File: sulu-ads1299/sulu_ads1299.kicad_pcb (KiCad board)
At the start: 2 copper layers, 32.5 x 42.8 mm, 76 parts, among them J1 Conn_01x08, J11 through_hole, J16 through_hole, J17 through_hole, J2 Conn_01x02, J20 through_hole, J3 Conn_02x05_Odd_Even, J4 through_hole, J5 through_hole, J6 through_hole, J8 through_hole, SW1 SW_DIP_x02, U1 TPS62222DDCT, U2 TLV71311PDBV, U3 LM2775DSG, U4 ADS1299_TQFP-64, U5 scum3

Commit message: Final submitted layout, gerbers, drill files, bom, and cpl
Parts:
- L2: footprint Inductor_SMD:L_Wuerth_MAPI-2010 -> Inductor_SMD:L_1008_2520Metric
- SW1: footprint Button_Switch_SMD:SW_DIP_SPSTx02_Slide_6.7x6.64mm_W6.73mm_P2.54mm_LowProfile_JPin -> eec:CK_Components-TDA02H0SB1-MFG
- moved U2 0.77 mm to (89.3, 68.7)
- moved C9 0.77 mm to (86.6, 68.2)
- moved C10 0.57 mm to (92.2, 68.2)
- moved L2 0.33 mm to (93.0, 72.1)
- moved SW1 0.13 mm to (113.2, 88.9)
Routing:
- net +1.8V_REG: track 86.1 -> 84.5 mm
- net +EXT_BAT: track 79.4 -> 78.1 mm
- net /~{ADS_PWDN}: track 22.1 -> 21.6 mm

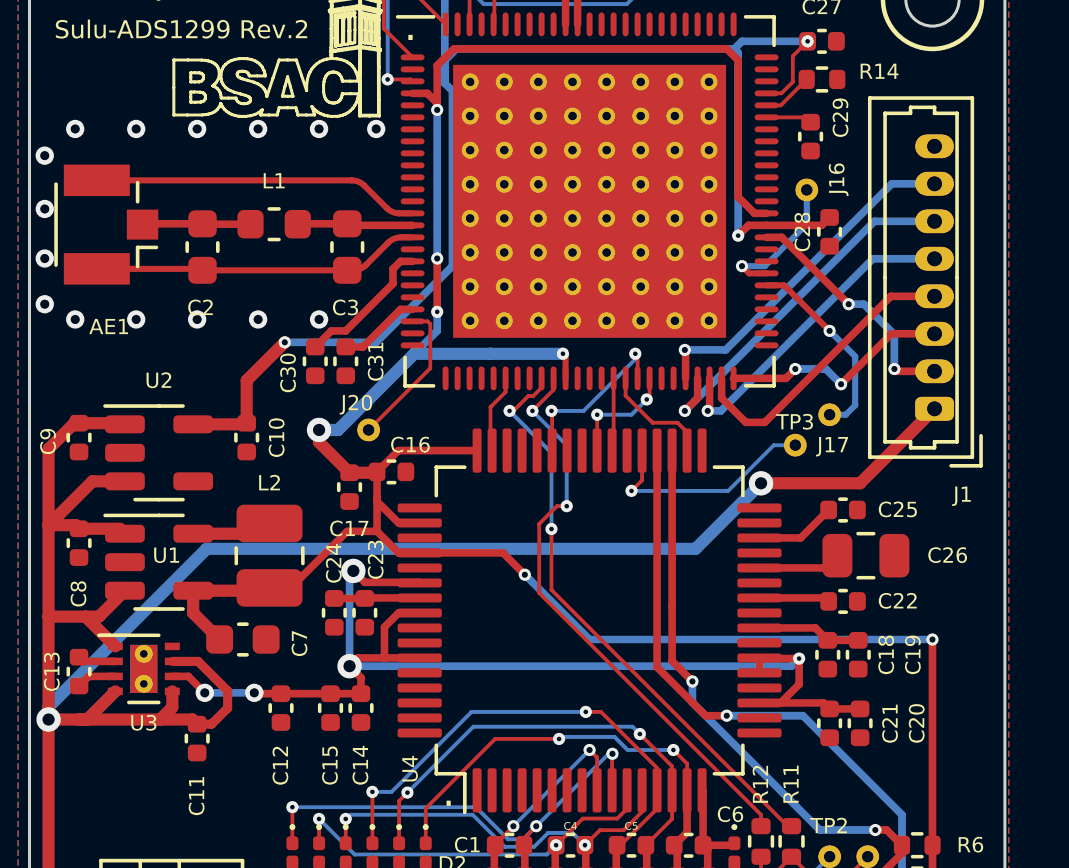
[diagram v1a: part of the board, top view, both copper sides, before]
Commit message: Sulu-ADS1299 Rev 3 improved routing surrounding QFN
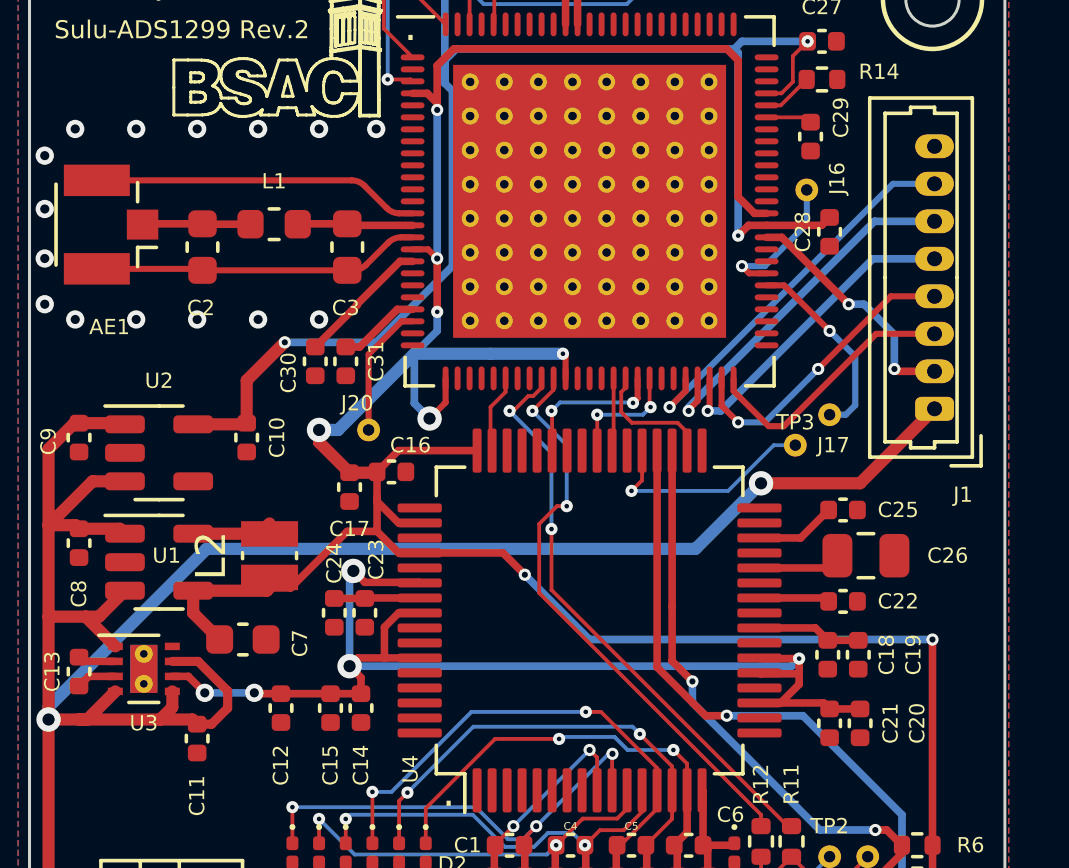
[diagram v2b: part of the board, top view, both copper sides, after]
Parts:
- L2: footprint Inductor_SMD:L_1008_2520Metric -> Inductor_SMD:L_Wuerth_MAPI-2010
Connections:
- U5 pad 17: unconnected-(U5-Pad17) -> +1.8V_REG
- U5 pad 26: unconnected-(U5-Pad26) -> +1.8V_REG
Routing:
- net +1.8V_REG: track 84.5 -> 89.3 mm, vias 7 -> 8
- net /RsTx: track 11.6 -> 13.1 mm
- net /3WB_DATA: track 7.73 -> 8.88 mm, vias 2 -> 0
- net +5V_REG: track 40.9 -> 41.7 mm
- net /SCUM_GPIO13: track 5.87 -> 5.05 mm
- net Net-(J20-Pad1): track 5.01 -> 4.44 mm
- net /SCUM_GPIO12: track 3.74 -> 4.27 mm
- net /3WB_ENB: track 9.83 -> 9.98 mm, vias 0 -> 2

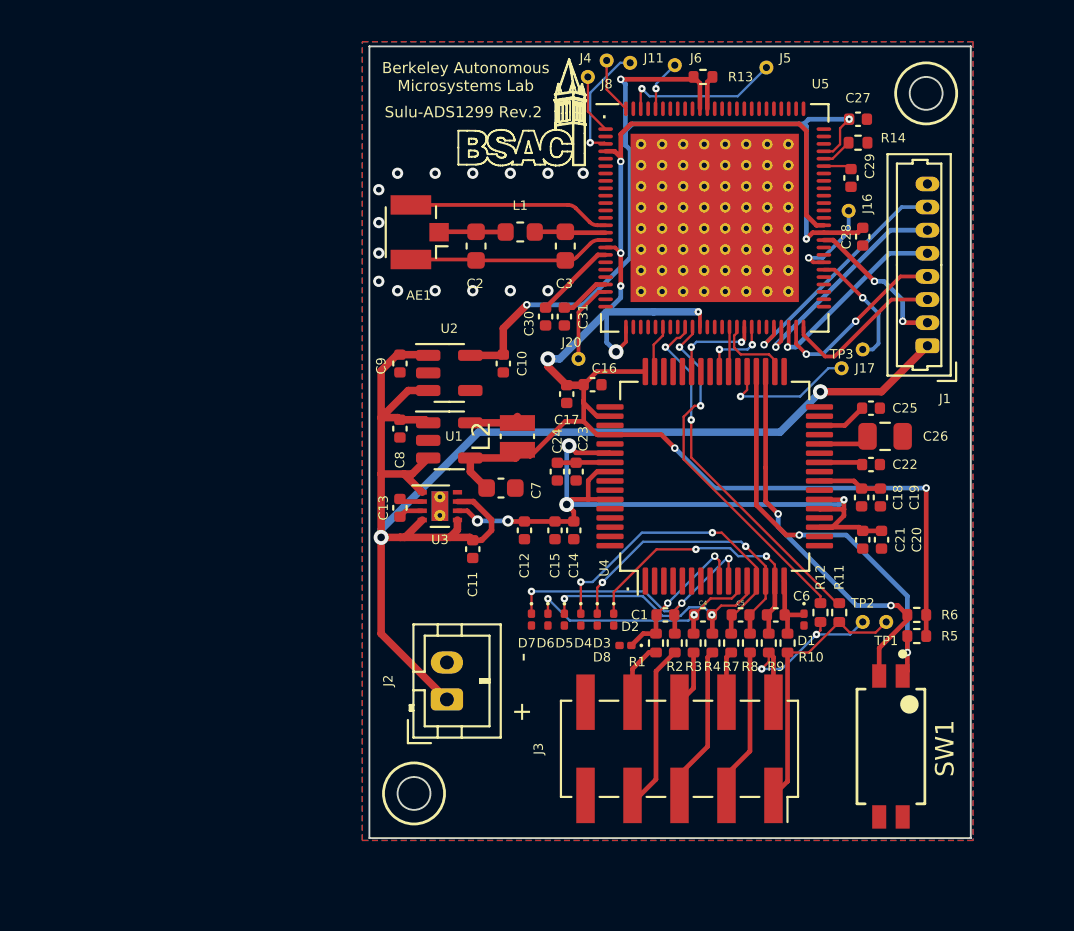
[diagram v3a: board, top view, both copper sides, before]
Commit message: Sulu-ADS1299 rev 3 fixed gpios, debug connector, two regulators
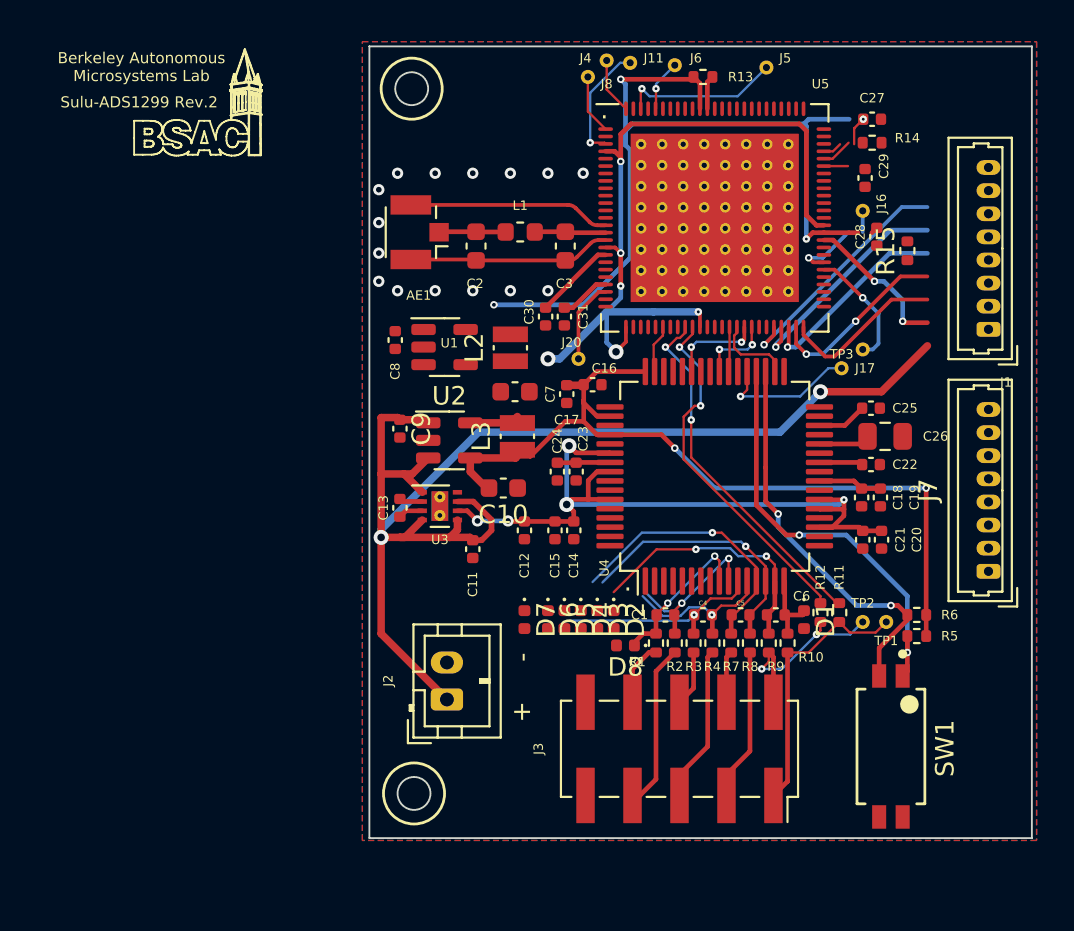
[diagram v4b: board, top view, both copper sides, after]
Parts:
- added J7: Conn_01x08, Molex Connectors:Molex_PicoBlade_53047-0810_1x08_P1.25mm_Vertical, F.Cu at (118.4, 79.4)
- added L3: 4.7 uH, Inductor_SMD:L_Wuerth_MAPI-2010, F.Cu at (93.0, 72.1)
- added R15: NP, Resistor_SMD:R_0402_1005Metric, F.Cu at (114.0, 62.1)
- C10: value 0.1 uF -> 22 uF; footprint Capacitor_SMD:C_0402_1005Metric -> Capacitor_SMD:C_0603_1608Metric
- C9: value 0.1 uF -> 4.7 uF
- D1, D2, D3, D4, D5, D6, D7, D8: footprint Diode_SMD:D_0201_0603Metric -> Diode_SMD:D_0402_1005Metric
- U2: value TLV71311PDBV -> TPS62222DDCT
- moved C10 6.73 mm to (92.2, 74.9), turned to 180 degrees
- moved C7 5.26 mm to (92.8, 69.7)
- moved U1 5.05 mm to (89.0, 67.3)
- moved L2 4.80 mm to (92.6, 67.3)
- moved C8 4.80 mm to (86.4, 66.9)
- moved U2 3.65 mm to (89.3, 72.4)
- moved C9 3.52 mm to (86.6, 71.7)
- moved J1 3.42 mm to (118.4, 66.4)
- moved C27 0.76 mm to (112.1, 55.0)
- moved C28 0.76 mm to (112.4, 61.3)
- moved C29 0.76 mm to (111.8, 58.2)
- moved J16 0.76 mm to (111.6, 59.9)
- moved R14 0.76 mm to (112.1, 56.3)
- moved D7 0.38 mm to (93.3, 82.0)
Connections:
- C10 pad 1: +1.1V_REG -> GND
- C10 pad 2: GND -> /+1.8V_ADS
- C16 pad 1: +1.8V_REG -> /+1.8V_ADS
- C17 pad 1: +1.8V_REG -> /+1.8V_ADS
- C27 pad 1: +1.1V_REG -> /SCuM-3C/+1.1V_REG
- C28 pad 1: +1.1V_REG -> /SCuM-3C/+1.1V_REG
- C7 pad 2: +1.8V_REG -> /+1.8V_SCUM
- L2 pad 1: +1.8V_REG -> /+1.8V_SCUM
- R11 pad 1: /SCUM_GPIO6 -> /SCUM_GPIO9
- R12 pad 1: /SCUM_GPIO7 -> /SCUM_GPIO10
- R13 pad 1: +1.1V_REG -> Net-(R13-Pad1)
- R5 pad 1: +1.8V_REG -> /+1.8V_SCUM
- R5 pad 2: /~{ADS_RESET} -> /SCUM_GPIO5
- R6 pad 1: +1.8V_REG -> /+1.8V_SCUM
- SW1 pad 1: /~{ADS_RESET} -> /SCUM_GPIO5
- U1 pad 4: +1.8V_REG -> /+1.8V_SCUM
- U2 pad 4: unconnected-(U2-Pad4) -> /+1.8V_ADS
- U2 pad 5: +1.1V_REG -> Net-(L3-Pad2)
- U4 pad 34: /SCUM_GPIO12 -> /SCUM_GPIO7
- U4 pad 36: /~{ADS_RESET} -> /SCUM_GPIO5
- U4 pad 39: /SCUM_GPIO11 -> /SCUM_GPIO4
- U4 pad 48: +1.8V_REG -> /+1.8V_ADS
- U4 pad 50: +1.8V_REG -> /+1.8V_ADS
- U4 pad 52: +1.8V_REG -> /+1.8V_ADS
- U5 pad 17: +1.8V_REG -> /+1.8V_SCUM
- U5 pad 26: +1.8V_REG -> /+1.8V_SCUM
- U5 pad 36: +1.8V_REG -> /+1.8V_SCUM
- U5 pad 4: +1.8V_REG -> /+1.8V_SCUM
- U5 pad 59: unconnected-(U5-Pad59) -> /+1.8V_SCUM
- U5 pad 61: +1.1V_REG -> /SCuM-3C/+1.1V_REG
- U5 pad 62: +1.8V_REG -> /+1.8V_SCUM
- U5 pad 72: +1.1V_REG -> /SCuM-3C/+1.1V_REG
- U5 pad 90: +1.1V_REG -> Net-(R13-Pad1)
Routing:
- net +1.8V_REG: track 89.3 -> 0.00 mm, vias 8 -> 0
- net /+1.8V_SCUM: track 0.00 -> 87.5 mm, vias 0 -> 8
- net +1.1V_REG: track 52.7 -> 0.00 mm, vias 4 -> 0
- net /SCuM-3C/+1.1V_REG: track 0.00 -> 49.4 mm, vias 0 -> 4
- net /~{ADS_RESET}: track 22.7 -> 0.00 mm, vias 2 -> 0
- net /SCUM_GPIO5: track 0.00 -> 22.7 mm, vias 0 -> 2
- net /SCUM_GPIO9: track 0.00 -> 19.5 mm, vias 0 -> 2
- net /SCUM_GPIO6: track 19.5 -> 0.00 mm, vias 2 -> 0
- net /SCUM_GPIO7: track 19.3 -> 0.00 mm, vias 2 -> 0
- net /SCUM_GPIO10: track 0.00 -> 19.3 mm, vias 0 -> 2
- net +EXT_BAT: track 78.1 -> 69.5 mm
- net /ADS_IN4P: track 16.5 -> 9.23 mm, vias 3 -> 2
- net /ADS_IN3P: track 13.8 -> 8.65 mm, vias 2 -> 1
- net Net-(L3-Pad2): track 0.00 -> 2.69 mm
- net Net-(L2-Pad2): track 2.69 -> 0.00 mm
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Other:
- board size 32.5 x 42.8 mm -> 35.8 x 42.8 mm

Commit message: Sulu-ADS1299 and connector board layout+sch progress
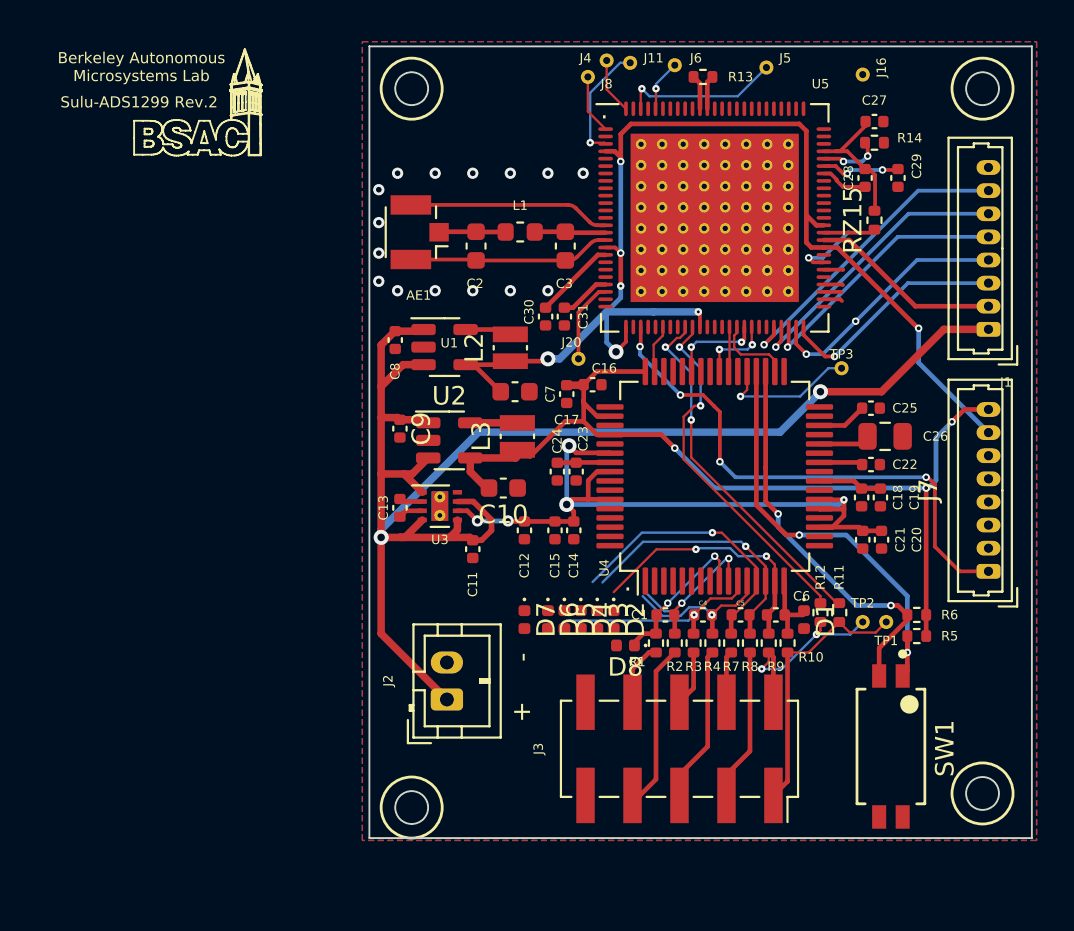
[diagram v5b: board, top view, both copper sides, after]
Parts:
- removed J17: through_hole, SCUM:through_hole
- removed R15: NP, Resistor_SMD:R_0402_1005Metric
- added RZ15: 0 Ohm, Resistor_SMD:R_0402_1005Metric, F.Cu at (112.3, 60.5)
- moved J16 7.37 mm to (111.6, 52.6)
- moved C28 3.24 mm to (111.8, 58.2)
- moved C29 1.78 mm to (113.5, 58.2)
- moved C27 0.18 mm to (112.3, 55.1)
- moved R14 0.13 mm to (112.3, 56.3)
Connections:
- R5 pad 1: /+1.8V_SCUM -> /+1.8V_ADS
- R6 pad 1: /+1.8V_SCUM -> /+1.8V_ADS
- U5 pad 56: Net-(J17-Pad1) -> unconnected-(U5-Pad56)
- U5 pad 61: /SCuM-3C/+1.1V_REG -> Net-(RZ15-Pad1)
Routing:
- net /+1.8V_ADS: track 0.00 -> 51.8 mm, vias 0 -> 3
- net /SCuM-3C/+1.1V_REG: track 49.4 -> 7.65 mm, vias 4 -> 0
- net /SCUM_GPIO0: track 0.00 -> 28.7 mm, vias 0 -> 4
- net /+1.8V_SCUM: track 87.5 -> 65.9 mm, vias 8 -> 7
- net +EXT_BAT: track 69.5 -> 82.5 mm
- net Net-(J17-Pad1): track 6.55 -> 0.00 mm, vias 1 -> 0
- net /SCUM_GPIO7: track 0.00 -> 4.27 mm
- net /SCUM_GPIO12: track 4.27 -> 0.00 mm
- net /RsTx: track 13.1 -> 16.8 mm
- net /3WB_ENB: track 9.98 -> 13.7 mm
- net /3WB_CLK: track 10.8 -> 14.4 mm
- net /3WB_DATA: track 8.88 -> 12.6 mm, vias 0 -> 1
- net /RsRx: track 12.2 -> 15.8 mm
- net Net-(RZ15-Pad1): track 0.00 -> 2.80 mm
- net Net-(C29-Pad1): track 1.53 -> 4.28 mm, vias 0 -> 2
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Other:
- outline, holes or cut-outs redrawn

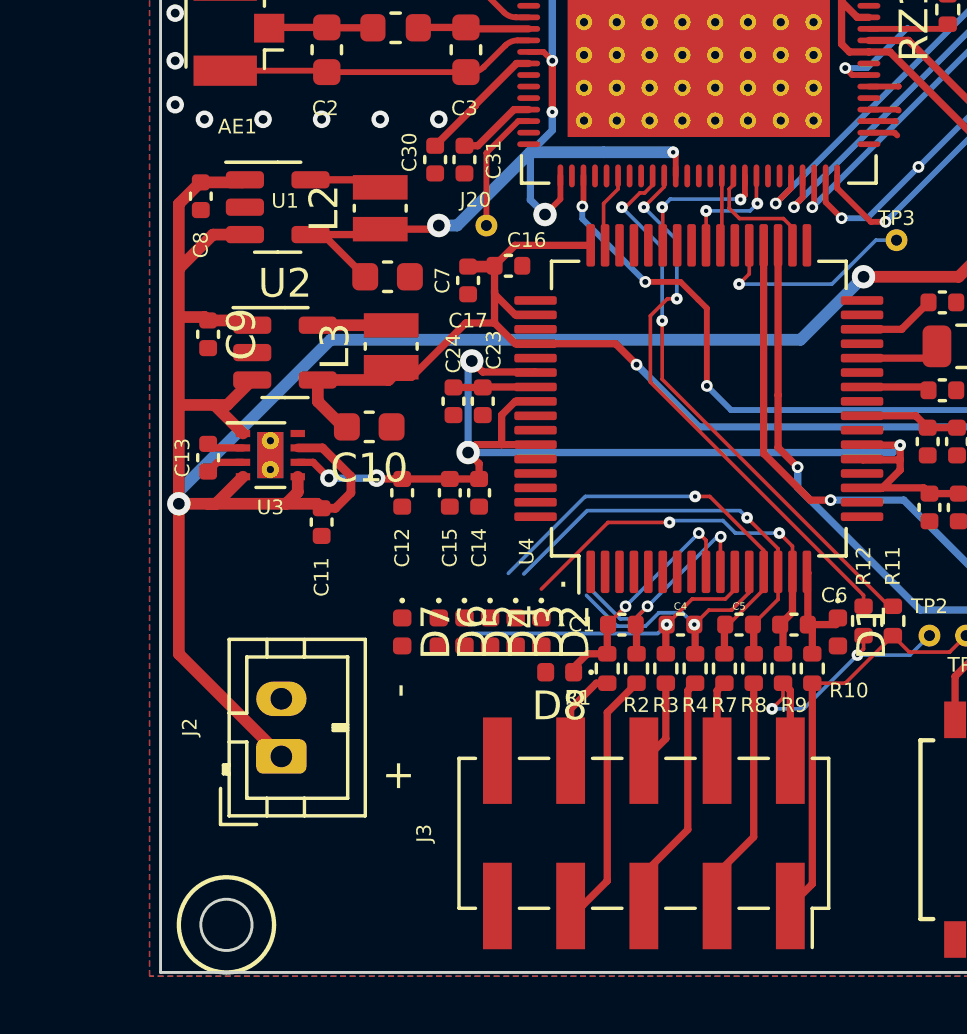
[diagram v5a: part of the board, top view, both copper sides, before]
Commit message: Sulu-ADS1299 mosfet input protection circuit
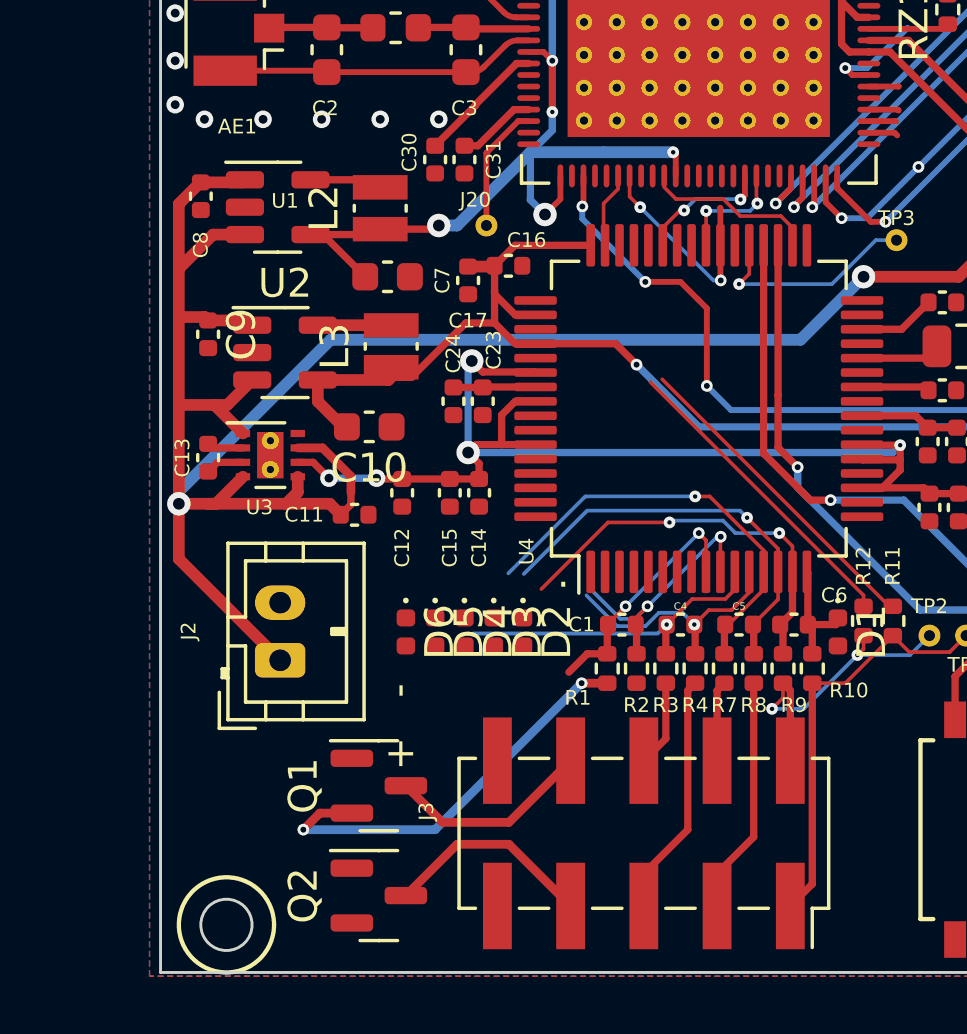
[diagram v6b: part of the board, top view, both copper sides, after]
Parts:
- removed D7, D8: GDZ5V1LP3-7, Diode_SMD:D_0402_1005Metric
- added Q1: BSS138, Package_TO_SOT_SMD:SOT-23, F.Cu at (92.5, 87.4)
- added Q2: BSS138, Package_TO_SOT_SMD:SOT-23, F.Cu at (92.5, 91.2)
- moved J2 3.33 mm to (89.1, 83.0)
- moved C11 1.17 mm to (91.7, 78.0), turned to 0 degrees
- moved D6 1.14 mm to (93.5, 82.0)
- moved D5 1.02 mm to (94.5, 82.0)
- moved D4 0.89 mm to (95.5, 82.0)
- moved D3 0.76 mm to (96.5, 82.0)
- moved D2 0.64 mm to (97.5, 82.0)
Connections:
- R1 pad 1: /ADS_IN4N_CONN -> Net-(R1-Pad1)
- R11 pad 1: /SCUM_GPIO9 -> /SCUM_GPIO1
- R12 pad 1: /SCUM_GPIO10 -> /SCUM_GPIO2
- R2 pad 1: /ADS_IN4P_CONN -> Net-(R2-Pad1)
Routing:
- net /SCUM_GPIO9: track 19.5 -> 0.00 mm, vias 2 -> 0
- net /SCUM_GPIO10: track 19.3 -> 0.00 mm, vias 2 -> 0
- net Net-(R1-Pad1): track 0.00 -> 14.6 mm, vias 0 -> 2
- net /SCUM_GPIO1: track 0.00 -> 11.3 mm
- net /SCUM_GPIO2: track 0.00 -> 10.8 mm
- net /SCUM_GPIO4: track 2.43 -> 7.68 mm, vias 0 -> 2
- net /ADS_IN4N_CONN: track 3.44 -> 7.13 mm
- net +EXT_BAT: track 82.5 -> 79.6 mm
- net /ADS_IN4P_CONN: track 8.91 -> 7.34 mm
- net /SCUM_GPIO7: track 4.27 -> 5.64 mm
